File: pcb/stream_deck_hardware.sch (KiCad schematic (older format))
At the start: 33 parts, among them J1 Conn_BOOT, J2 USB_C_Receptacle_USB2.0, J3 Conn_01x04_Male, J4 Conn_01x04_Male, U1 LF33_TO252, U2 STM32F401RCTx, U3 74LVC1G332, U4 AT24CS02-STUM, U5 AT24CS02-STUM, Y1 Crystal_Small

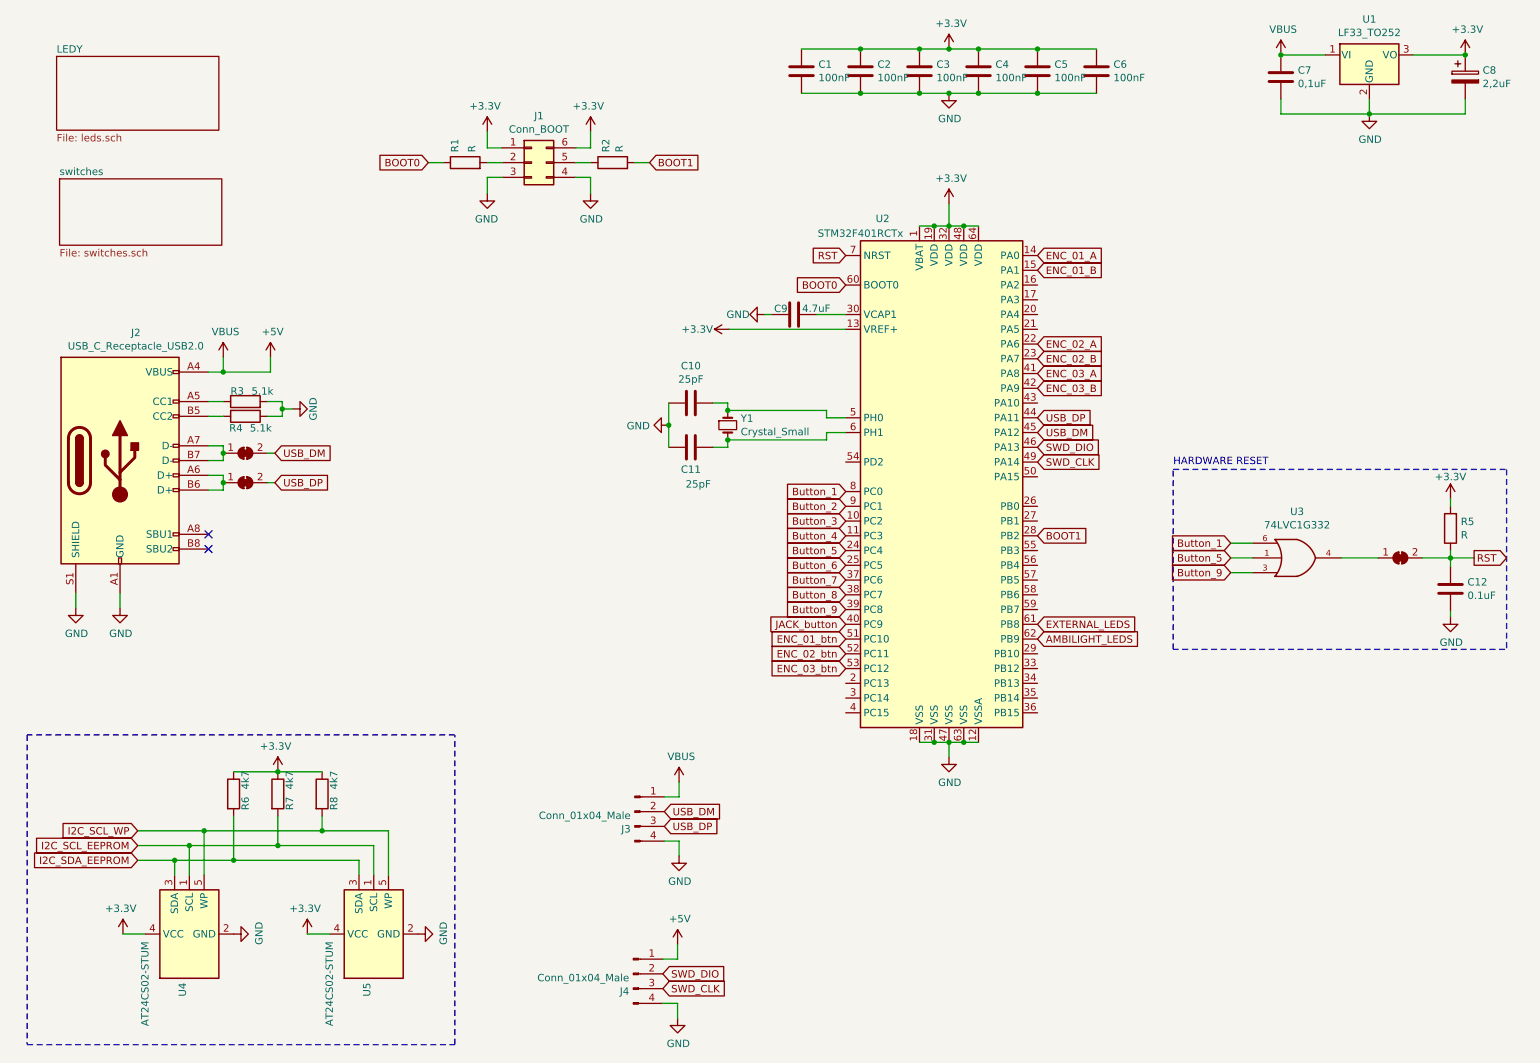
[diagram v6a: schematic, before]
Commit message: Footprints update and some changes
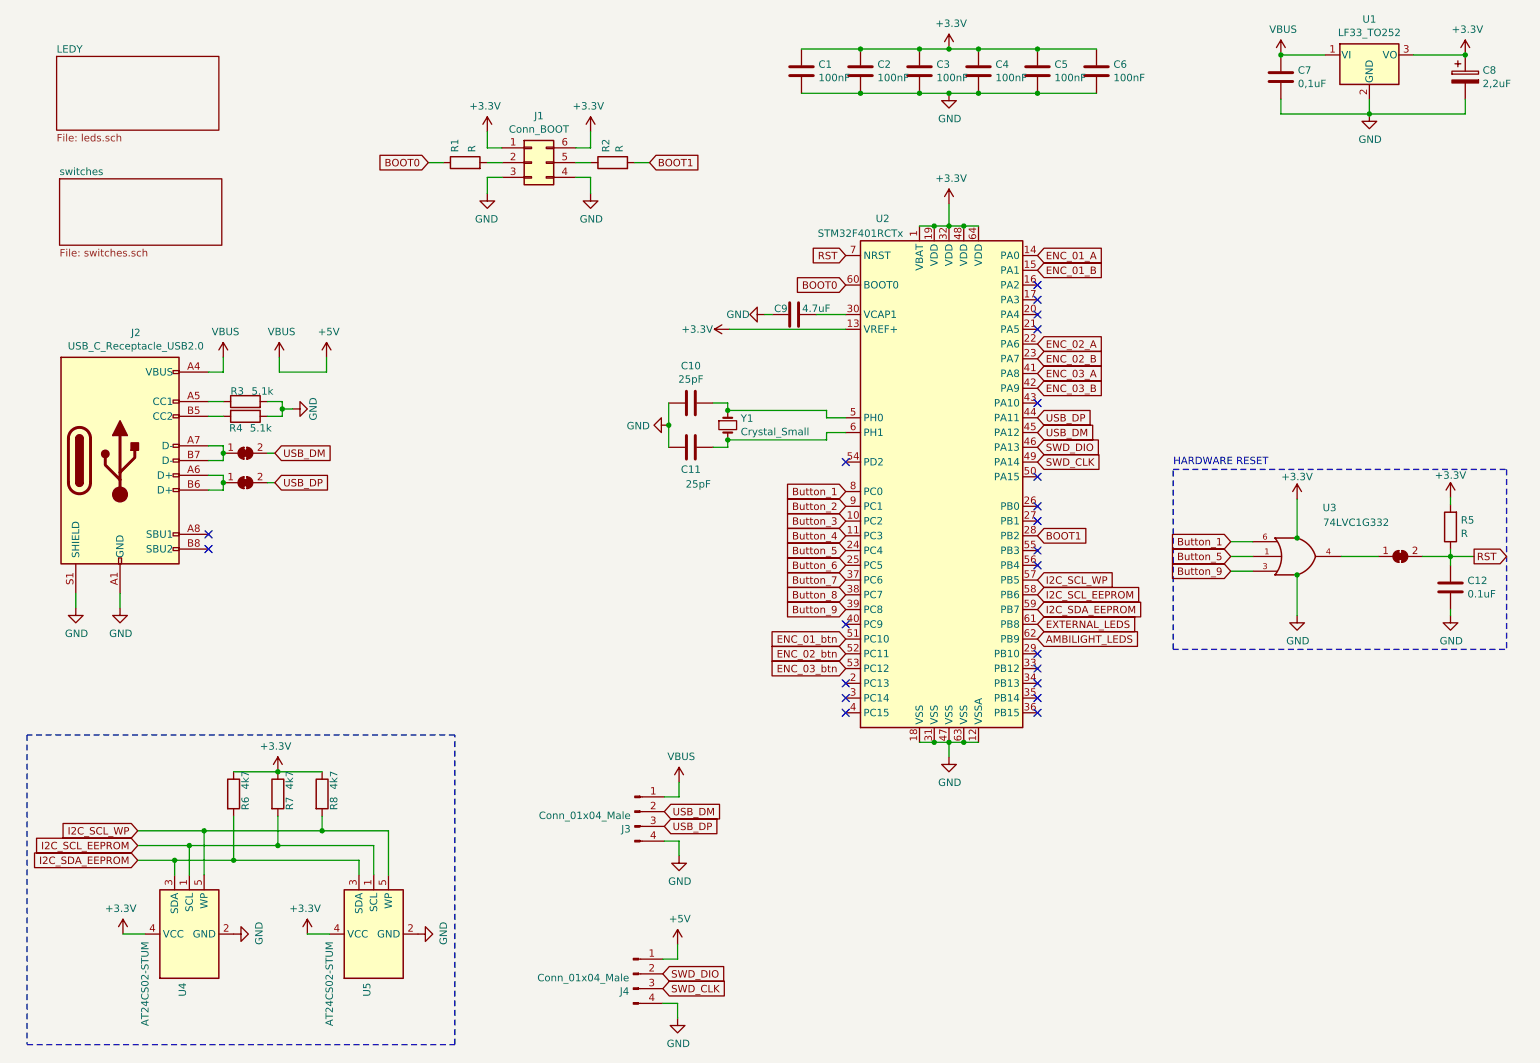
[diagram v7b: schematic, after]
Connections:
- net VCC is gone; now on net +3V3: U3.5 (VCC)
- net I2C_SCL_EEPROM: now also U2.58 (PB6)
- net I2C_SCL_WP: now also U2.57 (PB5)
- net I2C_SDA_EEPROM: now also U2.59 (PB7)
- net JACK_button: no longer names the net of U2.40 (PC9)
- no-connect marks 2 -> 22
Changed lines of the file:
@@
 Text GLabel 7550 3150 2    50   Input ~ 0
 ENC_03_B
-Text GLabel 6250 4750 0    50   Input ~ 0
-JACK_button
 Text GLabel 7550 2950 2    50   Input ~ 0
 ENC_02_B
@@
 Wire Wire Line
 	6120 3500 5450 3500
-Wire Wire Line
-	7150 5550 7050 5550
-Wire Wire Line
-	7050 5550 6950 5550
-Connection ~ 7050 5550
-Wire Wire Line
-	6850 5550 6950 5550
-Wire Wire Line
-	6750 5550 6850 5550
-Connection ~ 6850 5550
-Wire Wire Line
-	7150 2050 7050 2050
-Wire Wire Line
-	7050 2050 6950 2050
-Connection ~ 7050 2050
-Wire Wire Line
-	6850 2050 6950 2050
-Wire Wire Line
-	6750 2050 6850 2050
-Connection ~ 6850 2050
-$Comp
-L MCU_ST_STM32F4:STM32F401RCTx U2
-U 1 1 61BE2111
-P 6950 3750
-F 0 "U2" H 6500 5500 50  0000 C CNN
-F 1 "STM32F401RCTx" H 6350 5400 50  0000 C CNN
-F 2 "Package_QFP:LQFP-64_10x10mm_P0.5mm" H 6350 2050 50  0001 R CNN
-F 3 "http://www.st.com/st-web-ui/static/active/en/resource/technical/document/datasheet/DM00086815.pdf" H 6950 3750 50  0001 C CNN
-	1    6950 3750
-	1    0    0    -1
-$EndComp
 $Comp
 L power:GND #PWR011
@@
 	5460 2750 6250 2750
 Wire Wire Line
-	6050 2650 6250 2650
-Wire Wire Line
 	5750 2650 5700 2650
 $Comp
@@
 	0    -1   -1   0
 $EndComp
-$Comp
-L 74xGxx:74LVC1G332 U?
-U 1 1 61A443C9
-P 9310 4300
-AR Path="/61B99CE8/61A443C9" Ref="U?"  Part="1"
-AR Path="/61A443C9" Ref="U3"  Part="1"
-F 0 "U3" H 9310 4614 50  0000 C CNN
-F 1 "74LVC1G332" H 9310 4523 50  0000 C CNN
-F 2 "Package_TO_SOT_SMD:SOT-23-6" H 9310 4300 50  0001 C CNN
-F 3 "http://www.ti.com/lit/sg/scyt129e/scyt129e.pdf" H 9310 4300 50  0001 C CNN
-	1    9310 4300
-	1    0    0    -1
-$EndComp
-Text GLabel 8860 4200 0    50   Input ~ 0
+Text GLabel 8860 4190 0    50   Input ~ 0
 Button_1
-Text GLabel 8860 4300 0    50   Input ~ 0
+Text GLabel 8860 4290 0    50   Input ~ 0
 Button_5
-Text GLabel 8860 4400 0    50   Input ~ 0
+Text GLabel 8860 4390 0    50   Input ~ 0
 Button_9
 Wire Wire Line
-	8860 4200 9010 4200
-Wire Wire Line
-	8860 4300 9010 4300
-Wire Wire Line
-	8860 4400 9010 4400
-Text GLabel 10510 4300 2    50   Output ~ 0
+	8860 4190 9010 4190
+Wire Wire Line
+	8860 4290 9010 4290
+Wire Wire Line
+	8860 4390 9010 4390
+Text GLabel 10510 4290 2    50   Output ~ 0
 RST
 Text Notes 8470 3680 0    50   ~ 0
 HARDWARE RESET\n
 Wire Wire Line
-	10160 4300 10350 4300
-Wire Wire Line
-	9610 4300 9860 4300
+	10160 4290 10350 4290
+Wire Wire Line
+	9610 4290 9860 4290
 $Comp
 L Device:R R5
 U 1 1 61A47192
-P 10350 4100
-F 0 "R5" H 10280 4054 50  0000 R CNN
-F 1 "R" H 10280 4145 50  0000 R CNN
-F 2 "Resistor_SMD:R_0603_1608Metric" V 10280 4100 50  0001 C CNN
-F 3 "~" H 10350 4100 50  0001 C CNN
-	1    10350 4100
+P 10350 4090
+F 0 "R5" H 10280 4044 50  0000 R CNN
+F 1 "R" H 10280 4135 50  0000 R CNN
+F 2 "Resistor_SMD:R_0603_1608Metric" V 10280 4090 50  0001 C CNN
+F 3 "~" H 10350 4090 50  0001 C CNN
+	1    10350 4090
 	-1   0    0    1
 $EndComp
 Wire Wire Line
-	10350 4250 10350 4300
-Connection ~ 10350 4300
-Wire Wire Line
-	10350 4300 10510 4300
+	10350 4240 10350 4290
+Connection ~ 10350 4290
+Wire Wire Line
+	10350 4290 10510 4290
 $Comp
 L power:+3.3V #PWR017
 U 1 1 61A53414
-P 10350 3900
-F 0 "#PWR017" H 10350 3750 50  0001 C CNN
-F 1 "+3.3V" H 10350 4050 50  0000 C CNN
-F 2 "" H 10350 3900 50  0001 C CNN
-F 3 "" H 10350 3900 50  0001 C CNN
-	1    10350 3900
-	1    0    0    -1
-$EndComp
-Wire Wire Line
-	10350 3950 10350 3900
+P 10350 3890
+F 0 "#PWR017" H 10350 3740 50  0001 C CNN
+F 1 "+3.3V" H 10350 4040 50  0000 C CNN
+F 2 "" H 10350 3890 50  0001 C CNN
+F 3 "" H 10350 3890 50  0001 C CNN
+	1    10350 3890
+	1    0    0    -1
+$EndComp
+Wire Wire Line
+	10350 3940 10350 3890
 $Comp
 L Device:C C12
 U 1 1 61A6C3E1
-P 10350 4510
-F 0 "C12" H 10465 4556 50  0000 L CNN
-F 1 "0.1uF" H 10465 4465 50  0000 L CNN
-F 2 "Capacitor_SMD:C_0603_1608Metric" H 10388 4360 50  0001 C CNN
-F 3 "~" H 10350 4510 50  0001 C CNN
-	1    10350 4510
-	1    0    0    -1
-$EndComp
-Wire Wire Line
-	10350 4360 10350 4300
-Wire Wire Line
-	10350 4660 10350 4700
+P 10350 4500
+F 0 "C12" H 10465 4546 50  0000 L CNN
+F 1 "0.1uF" H 10465 4455 50  0000 L CNN
+F 2 "Capacitor_SMD:C_0603_1608Metric" H 10388 4350 50  0001 C CNN
+F 3 "~" H 10350 4500 50  0001 C CNN
+	1    10350 4500
+	1    0    0    -1
+$EndComp
+Wire Wire Line
+	10350 4350 10350 4290
+Wire Wire Line
+	10350 4650 10350 4690
 $Comp
 L power:GND #PWR020
 U 1 1 61A7259C
-P 10350 4700
-F 0 "#PWR020" H 10350 4450 50  0001 C CNN
-F 1 "GND" H 10355 4527 50  0000 C CNN
-F 2 "" H 10350 4700 50  0001 C CNN
-F 3 "" H 10350 4700 50  0001 C CNN
-	1    10350 4700
+P 10350 4690
+F 0 "#PWR020" H 10350 4440 50  0001 C CNN
+F 1 "GND" H 10355 4517 50  0000 C CNN
+F 2 "" H 10350 4690 50  0001 C CNN
+F 3 "" H 10350 4690 50  0001 C CNN
+	1    10350 4690
 	1    0    0    -1
 $EndComp
@@
 L power:+5V #PWR014
 U 1 1 61AE1ABA
-P 2350 2940
-F 0 "#PWR014" H 2350 2790 50  0001 C CNN
-F 1 "+5V" H 2365 3113 50  0000 C CNN
-F 2 "" H 2350 2940 50  0001 C CNN
-F 3 "" H 2350 2940 50  0001 C CNN
-	1    2350 2940
-	1    0    0    -1
-$EndComp
-Wire Wire Line
-	2030 3040 2350 3040
-Wire Wire Line
-	2350 3040 2350 2940
-Connection ~ 2030 3040
+P 2730 2940
+F 0 "#PWR014" H 2730 2790 50  0001 C CNN
+F 1 "+5V" H 2745 3113 50  0000 C CNN
+F 2 "" H 2730 2940 50  0001 C CNN
+F 3 "" H 2730 2940 50  0001 C CNN
+	1    2730 2940
+	1    0    0    -1
+$EndComp
+Wire Wire Line
+	2410 3040 2730 3040
+Wire Wire Line
+	2730 3040 2730 2940
 $Comp
 L power:VBUS #PWR023
@@
 L Jumper:SolderJumper_2_Bridged JP3
 U 1 1 61B5488E
-P 10010 4300
-F 0 "JP3" H 10010 4505 50  0001 C CNN
-F 1 "SolderJumper_2_Bridged" H 10010 4414 50  0001 C CNN
-F 2 "Jumper:SolderJumper-2_P1.3mm_Bridged2Bar_RoundedPad1.0x1.5mm" H 10010 4300 50  0001 C CNN
-F 3 "~" H 10010 4300 50  0001 C CNN
-	1    10010 4300
+P 10010 4290
+F 0 "JP3" H 10010 4495 50  0001 C CNN
+F 1 "SolderJumper_2_Bridged" H 10010 4404 50  0001 C CNN
+F 2 "Jumper:SolderJumper-2_P1.3mm_Bridged2Bar_RoundedPad1.0x1.5mm" H 10010 4290 50  0001 C CNN
+F 3 "~" H 10010 4290 50  0001 C CNN
+	1    10010 4290
 	1    0    0    -1
 $EndComp
@@
 Wire Notes Line
 	700  5500 700  7600
+$Comp
+L power:+3.3V #PWR0101
+U 1 1 61EA22FB
+P 9310 3900
+F 0 "#PWR0101" H 9310 3750 50  0001 C CNN
+F 1 "+3.3V" H 9310 4050 50  0000 C CNN
+F 2 "" H 9310 3900 50  0001 C CNN
+F 3 "" H 9310 3900 50  0001 C CNN
+	1    9310 3900
+	1    0    0    -1
+$EndComp
+Wire Wire Line
+	9310 4170 9310 4165
+$Comp
+L 74xGxx:74LVC1G332 U?
+U 1 1 61A443C9
+P 9310 4290
+AR Path="/61B99CE8/61A443C9" Ref="U?"  Part="1"
+AR Path="/61A443C9" Ref="U3"  Part="1"
+F 0 "U3" H 9530 4620 50  0000 C CNN
+F 1 "74LVC1G332" H 9710 4520 50  0000 C CNN
+F 2 "Package_TO_SOT_SMD:SOT-23-6" H 9310 4290 50  0001 C CNN
+F 3 "http://www.ti.com/lit/sg/scyt129e/scyt129e.pdf" H 9310 4290 50  0001 C CNN
+	1    9310 4290
+	1    0    0    -1
+$EndComp
+Connection ~ 9310 4165
+Wire Wire Line
+	9310 4165 9310 3900
+Wire Wire Line
+	9310 4410 9310 4415
+Connection ~ 9310 4415
+Wire Wire Line
+	9310 4415 9310 4690
+$Comp
+L power:GND #PWR0102
+U 1 1 61ED7E98
+P 9310 4690
+F 0 "#PWR0102" H 9310 4440 50  0001 C CNN
+F 1 "GND" H 9315 4517 50  0000 C CNN
+F 2 "" H 9310 4690 50  0001 C CNN
+F 3 "" H 9310 4690 50  0001 C CNN
+	1    9310 4690
+	1    0    0    -1
+$EndComp
+NoConn ~ 7550 2450
+NoConn ~ 7550 2550
+NoConn ~ 7550 2650
+NoConn ~ 7550 2750
+NoConn ~ 6250 3650
+NoConn ~ 7550 3750
+NoConn ~ 7550 3950
+NoConn ~ 7550 4050
+NoConn ~ 7550 4250
+NoConn ~ 7550 4350
+NoConn ~ 7550 4950
+NoConn ~ 7550 5050
+NoConn ~ 7550 5150
+Connection ~ 6850 2050
+Wire Wire Line
+	6850 2050 6950 2050
+Connection ~ 7050 2050
+Wire Wire Line
+	7050 2050 6950 2050
+Wire Wire Line
+	7150 2050 7050 2050
+Connection ~ 6850 5550
+Wire Wire Line
+	6850 5550 6950 5550
+Connection ~ 7050 5550
+Wire Wire Line
+	7050 5550 6950 5550
+Wire Wire Line
+	7150 5550 7050 5550
+Wire Wire Line
+	6750 5550 6850 5550
+Wire Wire Line
+	6750 2050 6850 2050
+$Comp
+L MCU_ST_STM32F4:STM32F401RCTx U2
+U 1 1 61BE2111
+P 6950 3750
+F 0 "U2" H 6500 5500 50  0000 C CNN
+F 1 "STM32F401RCTx" H 6350 5400 50  0000 C CNN
+F 2 "Package_QFP:LQFP-64_10x10mm_P0.5mm" H 6350 2050 50  0001 R CNN
+F 3 "http://www.st.com/st-web-ui/static/active/en/resource/technical/document/datasheet/DM00086815.pdf" H 6950 3750 50  0001 C CNN
+	1    6950 3750
+	1    0    0    -1
+$EndComp
+NoConn ~ 7550 5250
+NoConn ~ 7550 5350
+NoConn ~ 6250 5150
+NoConn ~ 6250 5250
+NoConn ~ 6250 5350
+NoConn ~ 6250 4750
+NoConn ~ 7550 3250
+Wire Wire Line
+	2410 3040 2410 2940
+$Comp
+L power:VBUS #PWR0103
+U 1 1 61F6CCF4
+P 2410 2940
+F 0 "#PWR0103" H 2410 2790 50  0001 C CNN
+F 1 "VBUS" H 2425 3113 50  0000 C CNN
+F 2 "" H 2410 2940 50  0001 C CNN
+F 3 "" H 2410 2940 50  0001 C CNN
+	1    2410 2940
+	1    0    0    -1
+$EndComp
+Text GLabel 7550 4650 2    50   Input ~ 0
+I2C_SDA_EEPROM
+Text GLabel 7550 4550 2    50   Input ~ 0
+I2C_SCL_EEPROM
+Text GLabel 7550 4450 2    50   Input ~ 0
+I2C_SCL_WP
+Wire Wire Line
+	6250 2650 6050 2650
 $EndSCHEMATC
